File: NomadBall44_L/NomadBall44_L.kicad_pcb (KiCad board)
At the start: 2 copper layers, 5.6 x 2.1 mm, 49 parts, among them SW1 SW_Push, SW10 SW_Push, SW11 SW_Push, SW12 SW_Push, SW13 SW_Push, SW14 SW_Push, SW15 SW_Push, SW16 SW_Push, SW17 SW_Push, SW18 SW_Push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

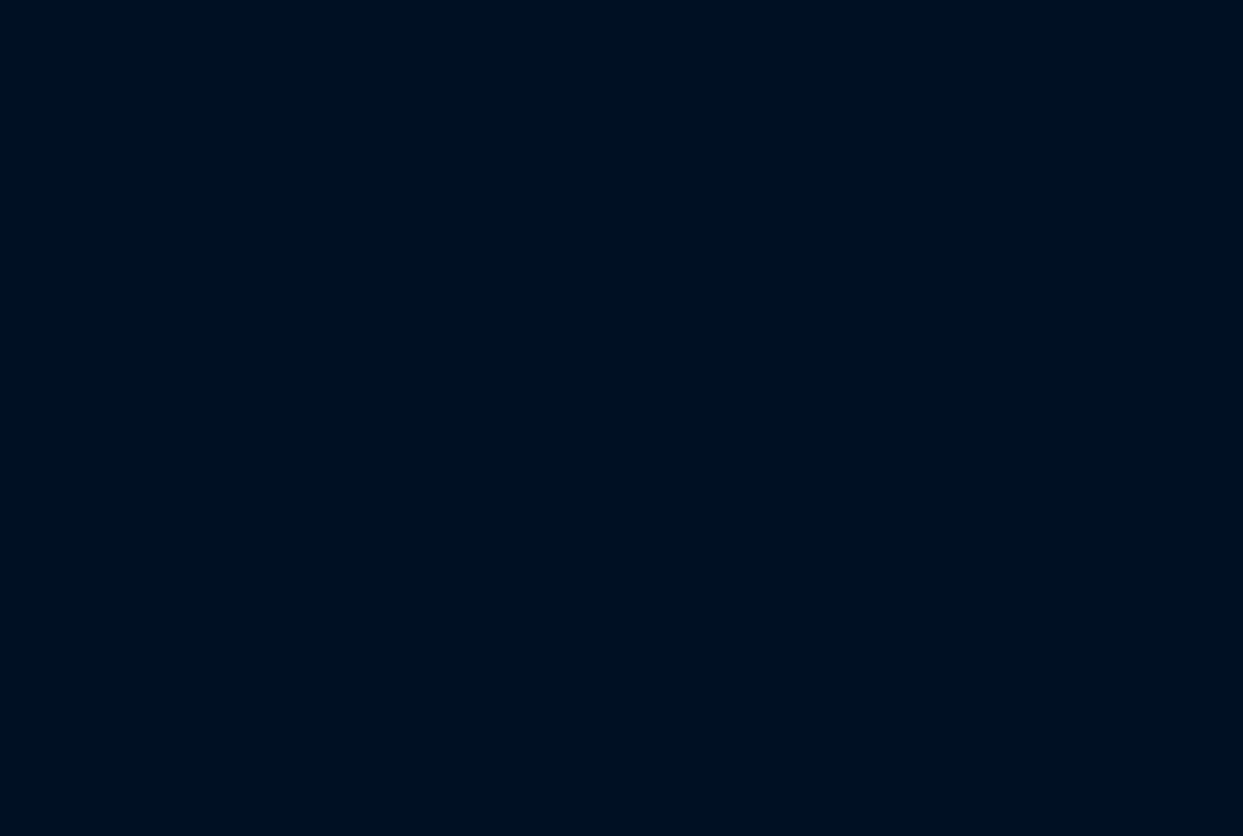
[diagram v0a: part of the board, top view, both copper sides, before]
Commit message: 右側PCBのレイアウトを反転さ左側PCBに配置
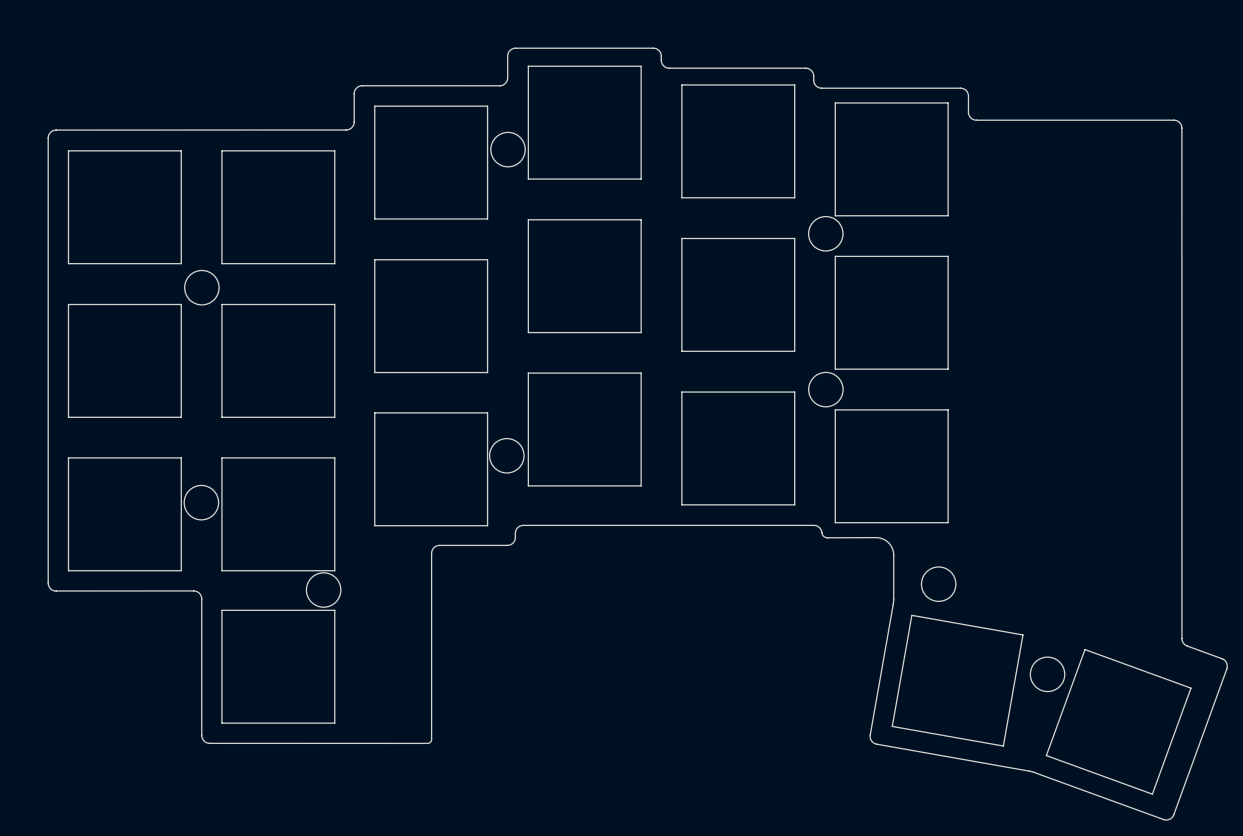
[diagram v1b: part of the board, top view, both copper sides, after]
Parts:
- added REF**: MountingHole_4.3mm_M4, MountingHole:MountingHole_4.3mm_M4, F.Cu at (244.8, 122.1)
- added REF**: MountingHole_4.3mm_M4, MountingHole:MountingHole_4.3mm_M4, F.Cu at (152.7, 112.0)
- added REF**: MountingHole_4.3mm_M4, MountingHole:MountingHole_4.3mm_M4, F.Cu at (167.9, 122.9)
- added REF**: MountingHole_4.3mm_M4, MountingHole:MountingHole_4.3mm_M4, F.Cu at (230.7, 78.3)
- added REF**: MountingHole_4.3mm_M4, MountingHole:MountingHole_4.3mm_M4, F.Cu at (191.0, 67.8)
- added REF**: MountingHole_4.3mm_M4, MountingHole:MountingHole_4.3mm_M4, F.Cu at (230.7, 97.8)
- added REF**: MountingHole_4.3mm_M4, MountingHole:MountingHole_4.3mm_M4, F.Cu at (190.8, 106.1)
- added REF**: MountingHole_4.3mm_M4, MountingHole:MountingHole_4.3mm_M4, F.Cu at (152.7, 85.1)
- added REF**: MountingHole_4.3mm_M4, MountingHole:MountingHole_4.3mm_M4, F.Cu at (258.4, 133.4)
- added SW1: SW_Push, NomadBall44:SW_Hole_1u, F.Cu at (239.0, 69.0)
- added SW10: SW_Push, NomadBall44:SW_Hole_1u, F.Cu at (181.4, 88.6)
- added SW11: SW_Push, NomadBall44:SW_Hole_1u, F.Cu at (162.3, 94.2)
- added SW12: SW_Push, NomadBall44:SW_Hole_1u, F.Cu at (143.1, 94.2)
- added SW13: SW_Push, NomadBall44:SW_Hole_1u, F.Cu at (239.0, 107.4)
- added SW14: SW_Push, NomadBall44:SW_Hole_1u, F.Cu at (219.8, 105.2)
- added SW15: SW_Push, NomadBall44:SW_Hole_1u, F.Cu at (200.6, 102.8)
- added SW16: SW_Push, NomadBall44:SW_Hole_1u, F.Cu at (181.4, 107.8)
- added SW17: SW_Push, NomadBall44:SW_Hole_1u, F.Cu at (162.3, 113.4)
- added SW18: SW_Push, NomadBall44:SW_Hole_1u, F.Cu at (143.1, 113.4)
- added SW19: SW_Push, NomadBall44:SW_Hole_1u, F.Cu at (267.3, 139.4)
- added SW2: SW_Push, NomadBall44:SW_Hole_1u, F.Cu at (219.8, 66.8)
- added SW20: SW_Push, NomadBall44:SW_Hole_1u, F.Cu at (247.2, 134.2)
- added SW22: SW_Push, NomadBall44:SW_Hole_1u, F.Cu at (162.3, 132.5)
- added SW3: SW_Push, NomadBall44:SW_Hole_1u, F.Cu at (200.6, 64.5)
- added SW4: SW_Push, NomadBall44:SW_Hole_1u, F.Cu at (181.4, 69.4)
- added SW5: SW_Push, NomadBall44:SW_Hole_1u, F.Cu at (162.3, 75.0)
- added SW6: SW_Push, NomadBall44:SW_Hole_1u, F.Cu at (143.1, 75.0)
- added SW7: SW_Push, NomadBall44:SW_Hole_1u, F.Cu at (239.0, 88.2)
- added SW8: SW_Push, NomadBall44:SW_Hole_1u, F.Cu at (219.8, 86.0)
- added SW9: SW_Push, NomadBall44:SW_Hole_1u, F.Cu at (200.6, 83.6)
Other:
- board size 5.6 x 2.1 mm -> 147.4 x 96.5 mm

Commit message: キースイッチを一部配置
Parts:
- moved SW19 232.5 mm to (267.3, 139.4), turned to -20 degrees
- moved SW20 209.6 mm to (247.2, 134.2), turned to -10 degrees
- moved SW1 200.5 mm to (239.0, 69.0)
- moved SW7 181.7 mm to (239.0, 88.2)
- moved SW2 178.8 mm to (219.8, 66.8)
- moved SW13 164.6 mm to (239.0, 107.4)
- moved SW8 160.8 mm to (219.8, 86.0)
- moved SW3 158.4 mm to (200.6, 64.5)
- moved SW14 139.6 mm to (219.8, 105.2)
- moved SW4 139.4 mm to (181.4, 69.4)
- moved SW9 135.1 mm to (200.6, 83.6)
- moved SW15 114.9 mm to (200.6, 102.8)
- moved SW10 113.4 mm to (181.4, 88.6)
- moved SW5 112.2 mm to (162.3, 75.0)
- moved SW17 97.7 mm to (162.3, 113.4)
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
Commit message: 外形線とスペーサーの位置を修正
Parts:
- removed the SW1 at (239.0, 69.0)
- removed the SW10 at (181.4, 88.6)
- removed the SW11 at (162.3, 94.2)
- removed the SW12 at (143.1, 94.2)
- removed the SW13 at (239.0, 107.4)
- removed the SW14 at (219.8, 105.2)
- removed the SW15 at (200.6, 102.8)
- removed the SW16 at (181.4, 107.8)
- removed the SW17 at (162.3, 113.4)
- removed the SW18 at (143.1, 113.4)
- removed the SW19 at (267.3, 139.4)
- removed the SW2 at (219.8, 66.8)
- removed the SW20 at (247.2, 134.2)
- removed the SW22 at (162.3, 132.5)
- removed the SW3 at (200.6, 64.5)
- removed the SW4 at (181.4, 69.4)
- removed the SW5 at (162.3, 75.0)
- removed the SW6 at (143.1, 75.0)
- removed the SW7 at (239.0, 88.2)
- removed the SW8 at (219.8, 86.0)
- removed the SW9 at (200.6, 83.6)
- moved SW21 187.1 mm to (226.4, 132.4)
- moved SW22 96.7 mm to (181.4, 127.0)
- moved SW23 76.2 mm to (162.3, 132.5)
- moved REF** 14.1 mm to (230.9, 119.9)
- moved REF** 5.64 mm to (190.8, 111.7)
- moved REF** 5.16 mm to (191.0, 62.7)
- moved REF** 2.43 mm to (170.3, 123.5)
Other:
- board size 147.4 x 96.5 mm -> 149 x 203 mm

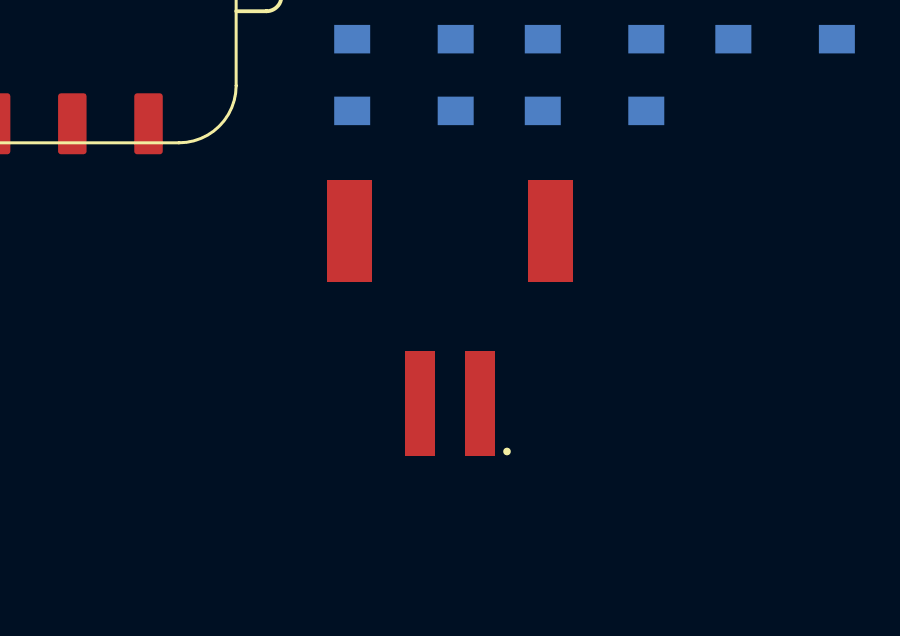
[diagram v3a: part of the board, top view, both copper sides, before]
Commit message: PHコネクタを反転
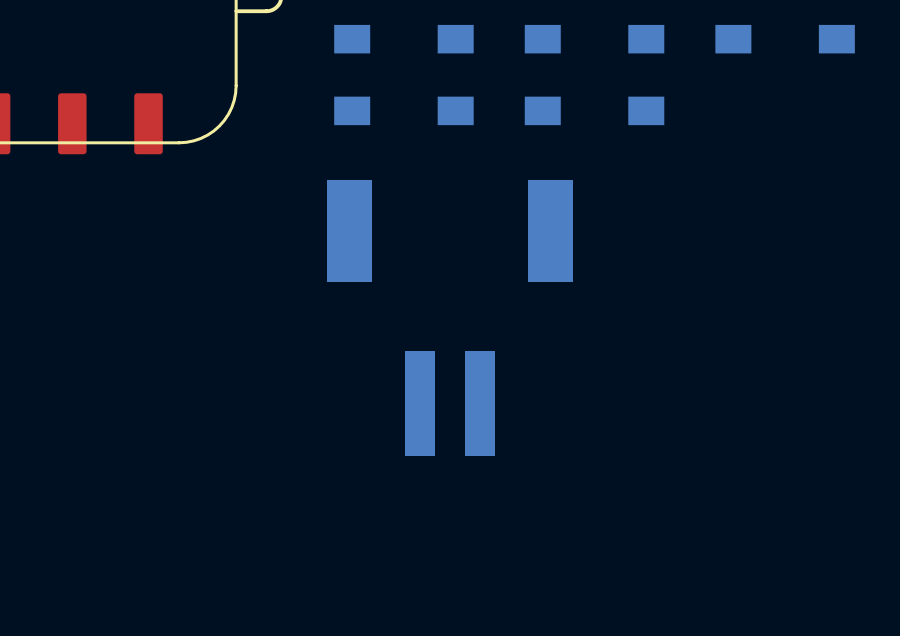
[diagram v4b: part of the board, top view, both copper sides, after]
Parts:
- BT1: moved to B.Cu
- turned BT1 to 180 degrees
